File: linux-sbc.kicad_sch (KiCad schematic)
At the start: 9 parts, among them J101 Molex Mini-fit Jr

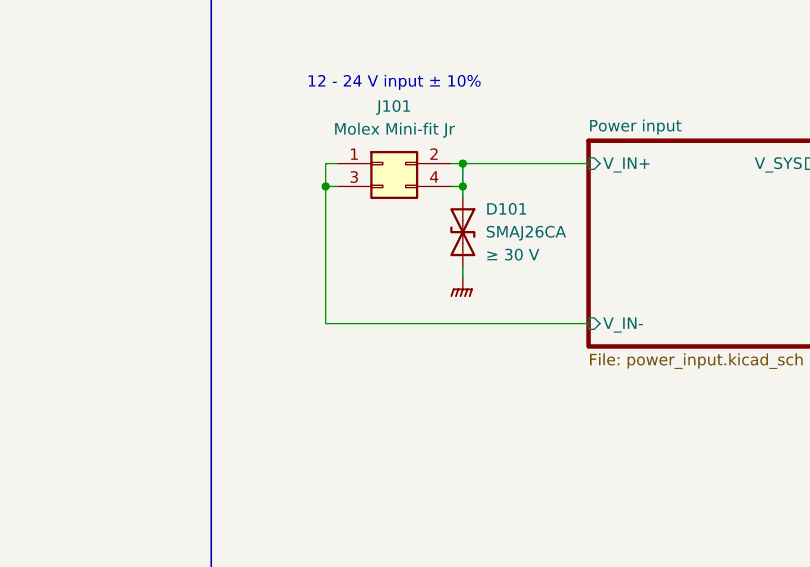
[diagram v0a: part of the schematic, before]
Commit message: Add series termination, assign netclasses, fill schemas' descriptions
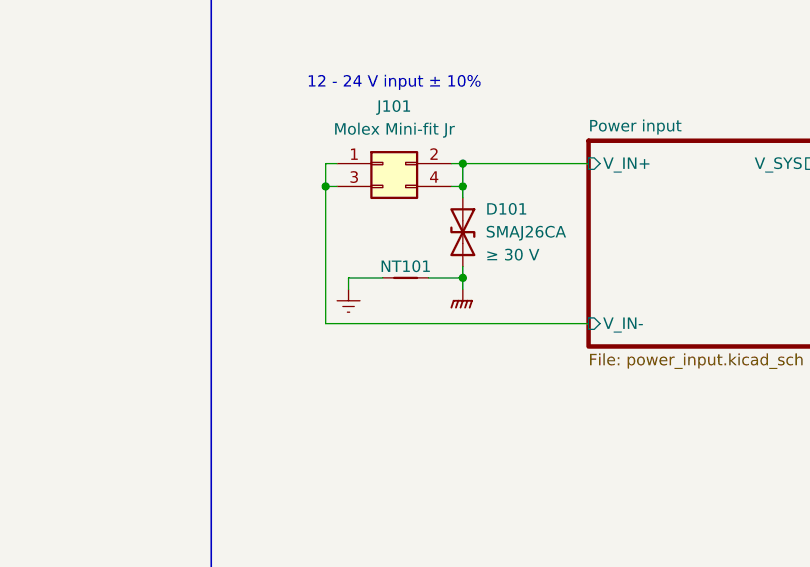
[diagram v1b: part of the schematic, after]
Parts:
- added NT101: NetTie_2, NetTie:NetTie-2_SMD_Pad2.0mm, symbol Device:NetTie_2
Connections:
- net CHASSIS: now also NT101.2
- new net GND: NT101.1
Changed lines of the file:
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@@
 			)
 			(justify left)
-			(href "#12")
+			(href "#13")
 		)
 	)
@@
 	)
 	(junction
+		(at 167.64 101.6)
+		(diameter 0)
+		(color 0 0 0 0)
+	)
+	(junction
 		(at 57.15 279.4)
 		(diameter 0)
@@
 	(wire
 		(pts
+			(xy 154.94 101.6) (xy 158.75 101.6)
+		)
+		(stroke
+			(width 0)
+			(type default)
+		)
+	)
+	(wire
+		(pts
 			(xy 44.45 278.13) (xy 44.45 279.4)
 		)
@@
 	(wire
 		(pts
+			(xy 167.64 101.6) (xy 167.64 102.87)
+		)
+		(stroke
+			(width 0)
+			(type default)
+		)
+	)
+	(wire
+		(pts
 			(xy 167.64 88.9) (xy 167.64 91.44)
 		)
@@
 	(wire
 		(pts
+			(xy 154.94 101.6) (xy 154.94 102.87)
+		)
+		(stroke
+			(width 0)
+			(type default)
+		)
+	)
+	(wire
+		(pts
 			(xy 57.15 280.67) (xy 57.15 279.4)
+		)
+		(stroke
+			(width 0)
+			(type default)
+		)
+	)
+	(wire
+		(pts
+			(xy 163.83 101.6) (xy 167.64 101.6)
 		)
 		(stroke
@@
 	)
 	(symbol
-		(lib_id "power:VCC")
-		(at 257.81 85.09 0)
-		(unit 1)
-		(exclude_from_sim no)
-		(in_bom yes)
-		(on_board yes)
-		(dnp no)
-		(property "Reference" "#PWR0103"
-			(at 257.81 88.9 0)
-			(effects
-				(font
-					(size 1.27 1.27)
-				)
-				(hide yes)
-			)
-		)
-		(property "Value" "V_3V3"
-			(at 257.81 82.042 0)
-			(effects
-				(font
-					(size 1.27 1.27)
-				)
-				(justify bottom)
-			)
-		)
-		(property "Footprint" ""
-			(at 257.81 85.09 0)
-			(effects
-				(font
-					(size 1.27 1.27)
-				)
-				(hide yes)
-			)
-		)
-		(property "Datasheet" ""
-			(at 257.81 85.09 0)
-			(effects
-				(font
-					(size 1.27 1.27)
-				)
-				(hide yes)
-			)
-		)
-		(property "Description" "Power symbol creates a global label with name \"VCC\""
-			(at 257.81 85.09 0)
-			(effects
-				(font
-					(size 1.27 1.27)
-				)
-				(hide yes)
-			)
-		)
-		(pin "1"
-		)
-		(instances
-			(project ""
-				(path "/fa11a02f-8043-4153-ab69-88d766503017"
-					(reference "#PWR0103")
-					(unit 1)
-				)
-			)
-		)
-	)
-	(symbol
-		(lib_id "power:GNDPWR")
-		(at 167.64 101.6 0)
+		(lib_id "power:Earth")
+		(at 154.94 102.87 0)
 		(unit 1)
 		(exclude_from_sim no)
@@
 		(fields_autoplaced yes)
 		(property "Reference" "#PWR0102"
-			(at 167.64 106.68 0)
-			(effects
-				(font
-					(size 1.27 1.27)
-				)
-				(hide yes)
-			)
-		)
-		(property "Value" "CHASSIS"
-			(at 167.513 105.41 0)
+			(at 154.94 109.22 0)
+			(effects
+				(font
+					(size 1.27 1.27)
+				)
+				(hide yes)
+			)
+		)
+		(property "Value" "GND"
+			(at 154.94 107.95 0)
 			(effects
 				(font
@@
 		)
 		(property "Footprint" ""
-			(at 167.64 102.87 0)
-			(effects
-				(font
-					(size 1.27 1.27)
-				)
-				(hide yes)
-			)
-		)
-		(property "Datasheet" ""
-			(at 167.64 102.87 0)
-			(effects
-				(font
-					(size 1.27 1.27)
-				)
-				(hide yes)
-			)
-		)
-		(property "Description" "Power symbol creates a global label with name \"GNDPWR\" , global ground"
-			(at 167.64 101.6 0)
+			(at 154.94 102.87 0)
+			(effects
+				(font
+					(size 1.27 1.27)
+				)
+				(hide yes)
+			)
+		)
+		(property "Datasheet" "~"
+			(at 154.94 102.87 0)
+			(effects
+				(font
+					(size 1.27 1.27)
+				)
+				(hide yes)
+			)
+		)
+		(property "Description" "Power symbol creates a global label with name \"Earth\""
+			(at 154.94 102.87 0)
 			(effects
 				(font
@@
 	)
 	(symbol
+		(lib_id "power:VCC")
+		(at 257.81 85.09 0)
+		(unit 1)
+		(exclude_from_sim no)
+		(in_bom yes)
+		(on_board yes)
+		(dnp no)
+		(property "Reference" "#PWR0104"
+			(at 257.81 88.9 0)
+			(effects
+				(font
+					(size 1.27 1.27)
+				)
+				(hide yes)
+			)
+		)
+		(property "Value" "V_3V3"
+			(at 257.81 82.042 0)
+			(effects
+				(font
+					(size 1.27 1.27)
+				)
+				(justify bottom)
+			)
+		)
+		(property "Footprint" ""
+			(at 257.81 85.09 0)
+			(effects
+				(font
+					(size 1.27 1.27)
+				)
+				(hide yes)
+			)
+		)
+		(property "Datasheet" ""
+			(at 257.81 85.09 0)
+			(effects
+				(font
+					(size 1.27 1.27)
+				)
+				(hide yes)
+			)
+		)
+		(property "Description" "Power symbol creates a global label with name \"VCC\""
+			(at 257.81 85.09 0)
+			(effects
+				(font
+					(size 1.27 1.27)
+				)
+				(hide yes)
+			)
+		)
+		(pin "1"
+		)
+		(instances
+			(project ""
+				(path "/fa11a02f-8043-4153-ab69-88d766503017"
+					(reference "#PWR0104")
+					(unit 1)
+				)
+			)
+		)
+	)
+	(symbol
+		(lib_id "power:GNDPWR")
+		(at 167.64 102.87 0)
+		(unit 1)
+		(exclude_from_sim no)
+		(in_bom yes)
+		(on_board yes)
+		(dnp no)
+		(fields_autoplaced yes)
+		(property "Reference" "#PWR0103"
+			(at 167.64 107.95 0)
+			(effects
+				(font
+					(size 1.27 1.27)
+				)
+				(hide yes)
+			)
+		)
+		(property "Value" "CHASSIS"
+			(at 167.513 106.68 0)
+			(effects
+				(font
+					(size 1.27 1.27)
+				)
+				(hide yes)
+			)
+		)
+		(property "Footprint" ""
+			(at 167.64 104.14 0)
+			(effects
+				(font
+					(size 1.27 1.27)
+				)
+				(hide yes)
+			)
+		)
+		(property "Datasheet" ""
+			(at 167.64 104.14 0)
+			(effects
+				(font
+					(size 1.27 1.27)
+				)
+				(hide yes)
+			)
+		)
+		(property "Description" "Power symbol creates a global label with name \"GNDPWR\" , global ground"
+			(at 167.64 102.87 0)
+			(effects
+				(font
+					(size 1.27 1.27)
+				)
+				(hide yes)
+			)
+		)
+		(pin "1"
+		)
+		(instances
+			(project "linux-sbc"
+				(path "/fa11a02f-8043-4153-ab69-88d766503017"
+					(reference "#PWR0103")
+					(unit 1)
+				)
+			)
+		)
+	)
+	(symbol
 		(lib_id "Mechanical:Fiducial")
 		(at 101.6 274.32 0)
@@
 		(on_board yes)
 		(dnp no)
-		(property "Reference" "#PWR0104"
+		(property "Reference" "#PWR0105"
 			(at 266.7 88.9 0)
 			(effects
@@
 			(project "linux-sbc"
 				(path "/fa11a02f-8043-4153-ab69-88d766503017"
-					(reference "#PWR0104")
+					(reference "#PWR0105")
 					(unit 1)
 				)
@@
 					(unit 1)
 				)
+			)
+		)
+	)
+	(symbol
+		(lib_id "Device:NetTie_2")
+		(at 161.29 101.6 0)
+		(unit 1)
+		(exclude_from_sim no)
+		(in_bom no)
+		(on_board yes)
+		(dnp no)
+		(property "Reference" "NT101"
+			(at 161.29 101.092 0)
+			(effects
+				(font
+					(size 1.27 1.27)
+				)
+				(justify bottom)
+			)
+		)
+		(property "Value" "NetTie_2"
+			(at 161.29 101.092 0)
+			(effects
+				(font
+					(size 1.27 1.27)
+				)
+				(justify bottom)
+				(hide yes)
+			)
+		)
+		(property "Footprint" "NetTie:NetTie-2_SMD_Pad2.0mm"
+			(at 161.29 101.6 0)
+			(effects
+				(font
+					(size 1.27 1.27)
+				)
+				(hide yes)
+			)
+		)
+		(property "Datasheet" "~"
+			(at 161.29 101.6 0)
+			(effects
+				(font
+					(size 1.27 1.27)
+				)
+				(hide yes)
+			)
+		)
+		(property "Description" "Net tie, 2 pins"
+			(at 161.29 101.6 0)
+			(effects
+				(font
+					(size 1.27 1.27)
+				)
+				(hide yes)
+			)
+		)
+		(pin "1"
+		)
+		(pin "2"
+		)
+		(instances
+			(project ""
+				(path "/fa11a02f-8043-4153-ab69-88d766503017"
+					(reference "NT101")
+					(unit 1)
+				)

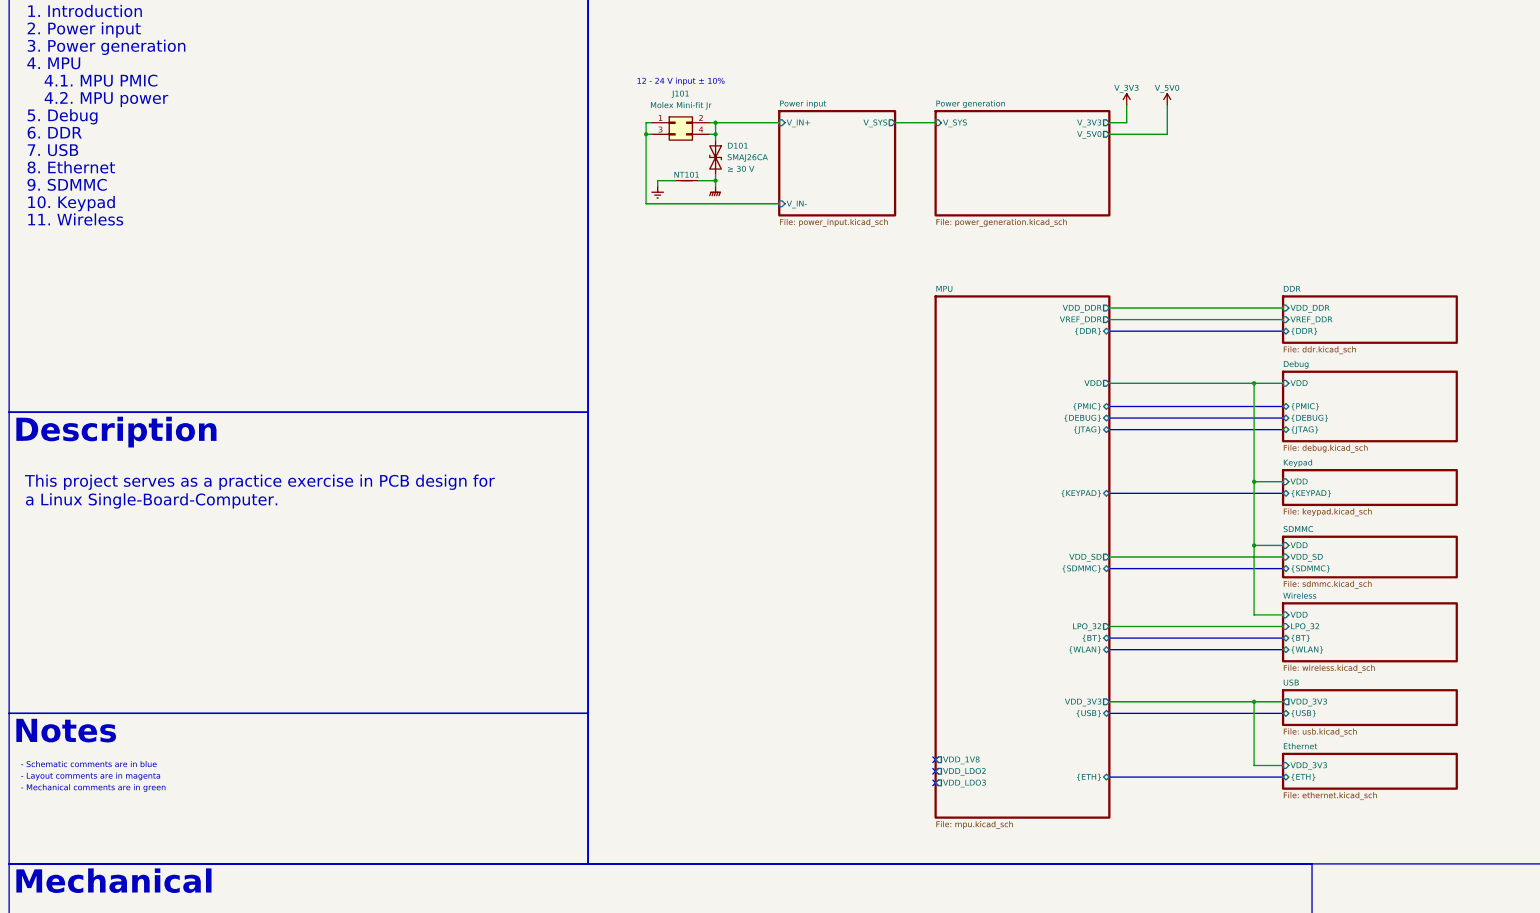
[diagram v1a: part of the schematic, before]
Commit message: Add LCD screen
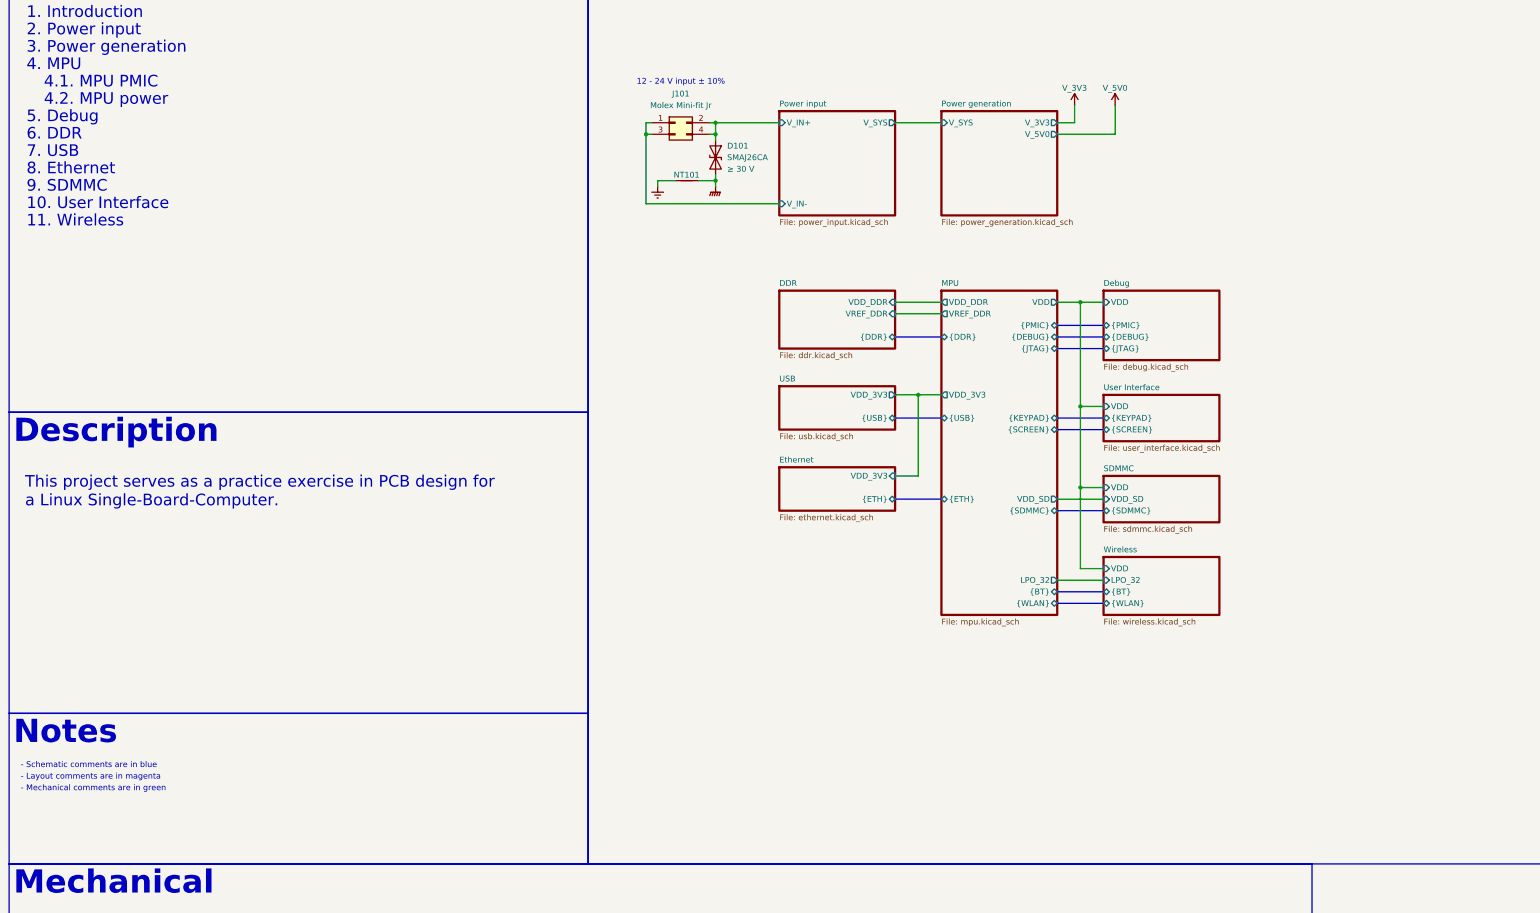
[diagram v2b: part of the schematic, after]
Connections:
- no-connect marks 3 -> 0
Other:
- sheet Keypad renamed User Interface
- sheet MPU ports: added {SCREEN}; removed VDD_1V8, VDD_LDO2, VDD_LDO3
- sheet User Interface: file keypad.kicad_sch -> user_interface.kicad_sch
- sheet User Interface ports: added {SCREEN}; removed none
- note added: "10. User Interface"
- note removed: "10. Keypad"

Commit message: Refactor symbol properties
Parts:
- D101: DigiKey Part Number 732-SMAJ26CACT-ND -> (none)
- J101: DigiKey Part Number 0455860005-ND -> (none)
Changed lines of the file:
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@@
-			)
-		)
-		(property "DigiKey Part Number" "0455860005-ND"
-			(at 158.75 88.9 0)
-			(effects
-				(font
-					(size 1.27 1.27)
-				)
-				(hide yes)
 			)
 		)
@@
 			)
 		)
-		(property "Power" ""
-			(at 158.75 88.9 0)
-			(effects
-				(font
-					(size 1.27 1.27)
-				)
-				(hide yes)
-			)
-		)
-		(property "Temperature Coefficient" ""
-			(at 158.75 88.9 0)
-			(effects
-				(font
-					(size 1.27 1.27)
-				)
-				(hide yes)
-			)
-		)
 		(pin "2"
 		)
@@
 			)
 		)
-		(property "Power" ""
-			(at 38.1 275.59 0)
-			(effects
-				(font
-					(size 1.27 1.27)
-				)
-				(hide yes)
-			)
-		)
-		(property "Temperature Coefficient" ""
-			(at 38.1 275.59 0)
-			(effects
-				(font
-					(size 1.27 1.27)
-				)
-				(hide yes)
-			)
-		)
 		(pin "1"
 		)
@@
 		)
 		(property "Footprint review check" "+"
-			(at 50.8 275.59 0)
-			(effects
-				(font
-					(size 1.27 1.27)
-				)
-				(hide yes)
-			)
-		)
-		(property "Power" ""
-			(at 50.8 275.59 0)
-			(effects
-				(font
-					(size 1.27 1.27)
-				)
-				(hide yes)
-			)
-		)
-		(property "Temperature Coefficient" ""
 			(at 50.8 275.59 0)
 			(effects
@@
 			)
 		)
-		(property "Power" ""
-			(at 101.6 274.32 0)
-			(effects
-				(font
-					(size 1.27 1.27)
-				)
-				(hide yes)
-			)
-		)
-		(property "Temperature Coefficient" ""
-			(at 101.6 274.32 0)
-			(effects
-				(font
-					(size 1.27 1.27)
-				)
-				(hide yes)
-			)
-		)
 		(instances
 			(project "linux-sbc"
@@
 			)
 		)
-		(property "Power" ""
-			(at 88.9 274.32 0)
-			(effects
-				(font
-					(size 1.27 1.27)
-				)
-				(hide yes)
-			)
-		)
-		(property "Temperature Coefficient" ""
-			(at 88.9 274.32 0)
-			(effects
-				(font
-					(size 1.27 1.27)
-				)
-				(hide yes)
-			)
-		)
 		(instances
 			(project "linux-sbc"
@@
 		)
 		(property "Footprint review check" "+"
-			(at 57.15 275.59 0)
-			(effects
-				(font
-					(size 1.27 1.27)
-				)
-				(hide yes)
-			)
-		)
-		(property "Power" ""
-			(at 57.15 275.59 0)
-			(effects
-				(font
-					(size 1.27 1.27)
-				)
-				(hide yes)
-			)
-		)
-		(property "Temperature Coefficient" ""
 			(at 57.15 275.59 0)
 			(effects
@@
 			)
 		)
-		(property "Power" ""
-			(at 114.3 274.32 0)
-			(effects
-				(font
-					(size 1.27 1.27)
-				)
-				(hide yes)
-			)
-		)
-		(property "Temperature Coefficient" ""
-			(at 114.3 274.32 0)
-			(effects
-				(font
-					(size 1.27 1.27)
-				)
-				(hide yes)
-			)
-		)
 		(instances
 			(project "linux-sbc"
@@
 			)
 		)
-		(property "DigiKey Part Number" "732-SMAJ26CACT-ND"
-			(at 167.64 96.52 90)
-			(effects
-				(font
-					(size 1.27 1.27)
-				)
-				(hide yes)
-			)
-		)
 		(property "Manufacturer" "Würth Elektronik"
 			(at 167.64 96.52 90)
@@
 				)
 				(justify left)
-			)
-		)
-		(property "Temperature Coefficient" ""
-			(at 167.64 96.52 90)
-			(effects
-				(font
-					(size 1.27 1.27)
-				)
-				(hide yes)
 			)
 		)
@@
 			(at 44.45 275.59 0)
 			(effects
-				(font
-					(size 1.27 1.27)
-				)
-				(hide yes)
-			)
-		)
-		(property "Power" ""
-			(at 44.45 275.59 0)
-			(effects
-				(font
-					(size 1.27 1.27)
-				)
-				(hide yes)
-			)
-		)
-		(property "Temperature Coefficient" ""
-			(at 44.45 275.59 0)
-			(effects

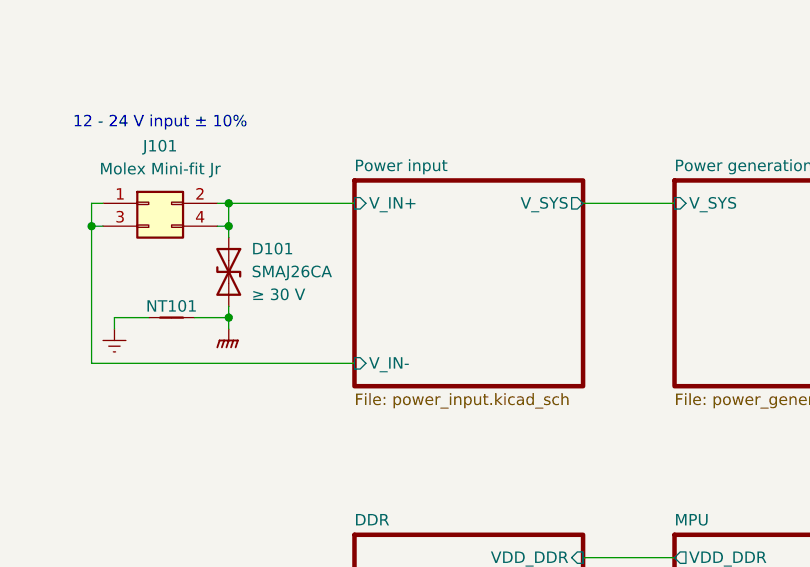
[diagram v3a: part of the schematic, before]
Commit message: Refactor schematics
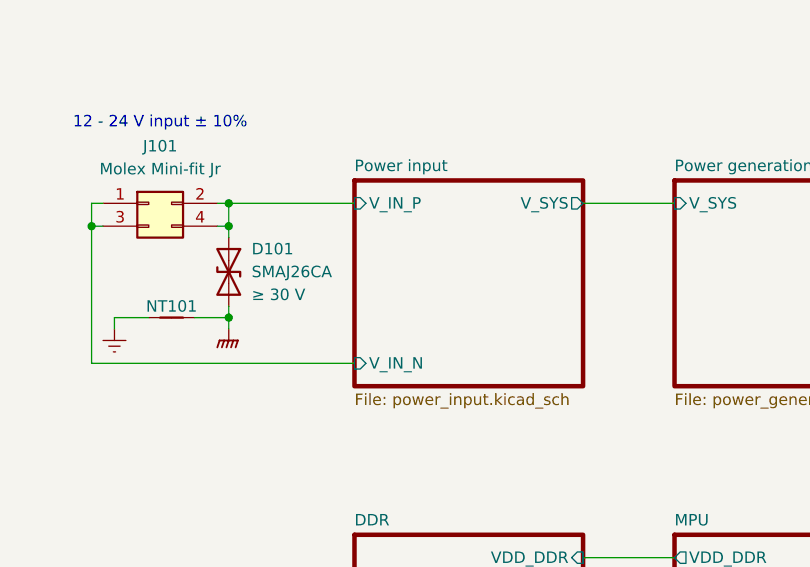
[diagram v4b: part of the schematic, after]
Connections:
- net Power input/V_IN+ renamed Power input/V_IN_P
- net Power input/V_IN- renamed Power input/V_IN_N
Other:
- sheet Power input ports: added V_IN_N, V_IN_P; removed V_IN+, V_IN-
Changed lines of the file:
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@@
 			)
 		)
-		(pin "V_IN+" input
+		(pin "V_IN_P" input
 			(at 181.61 88.9 180)
 			(effects
@@
 			)
 		)
-		(pin "V_IN-" input
+		(pin "V_IN_N" input
 			(at 181.61 106.68 180)
 			(effects
